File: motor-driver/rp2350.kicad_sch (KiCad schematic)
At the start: 39 parts, among them J2 SM03B-SRSS-TB, U10 W25Q128JVS, U12 NCP1117-3.3_SOT223, U13 RP2350_80QFN, Y1 ABM8-272-T3

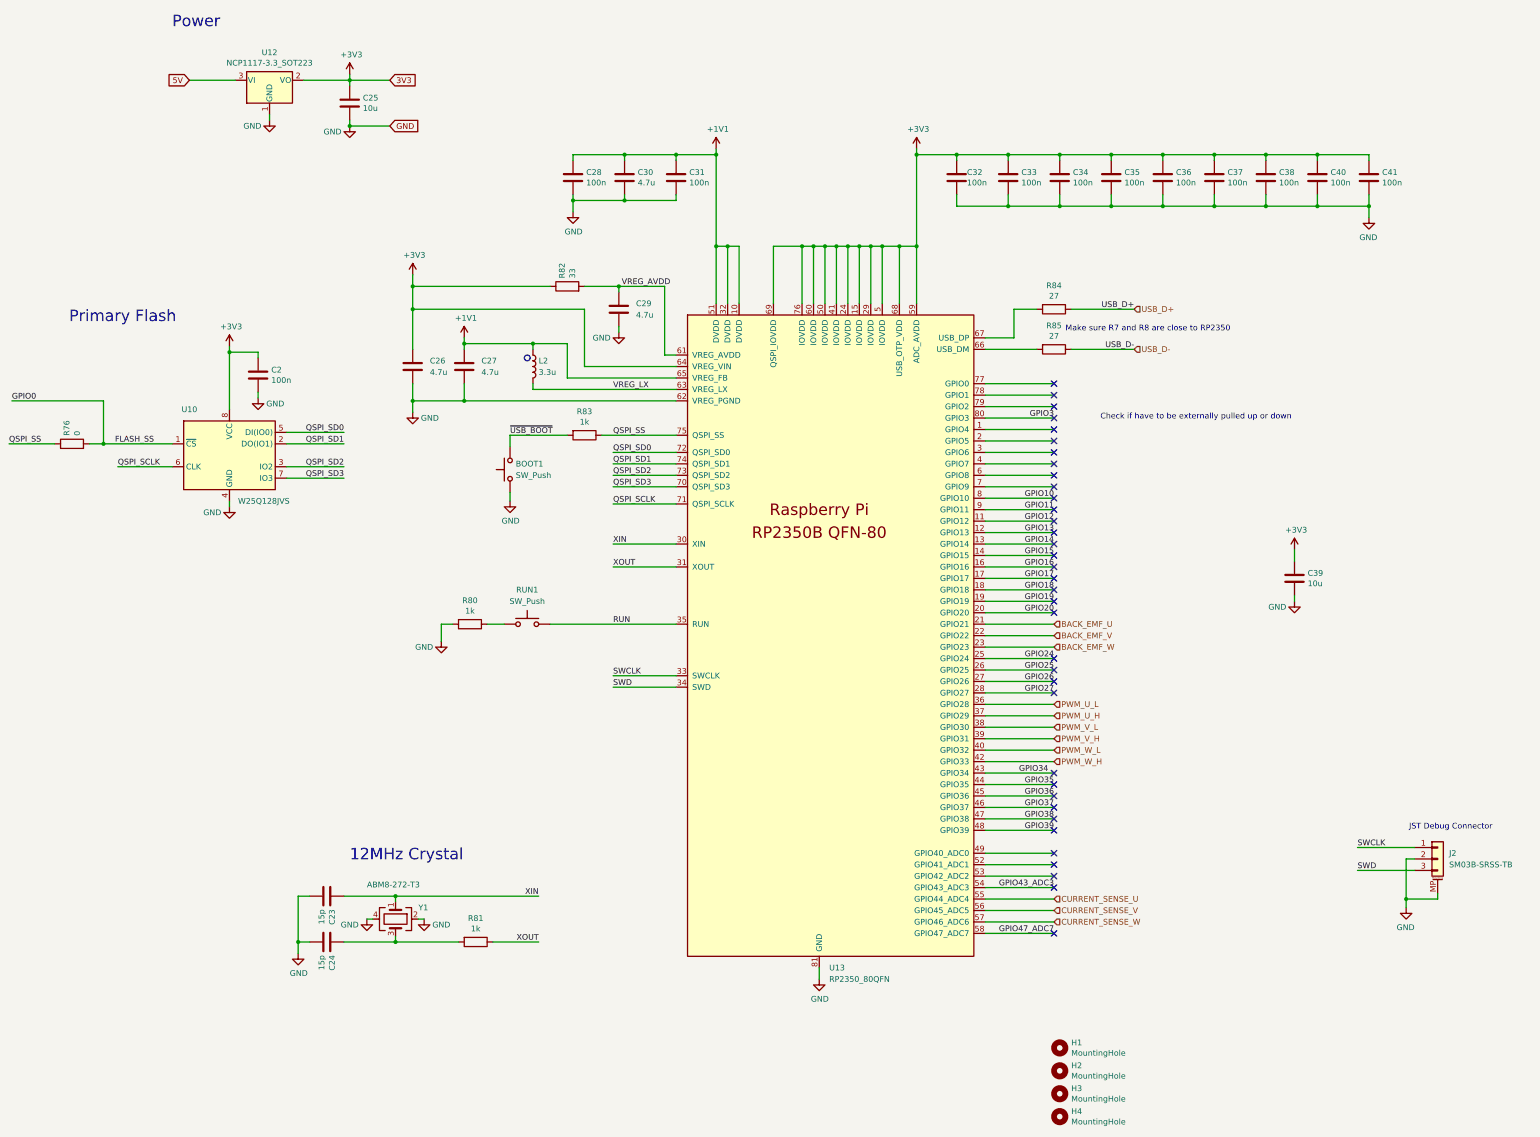
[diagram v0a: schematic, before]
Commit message: added spi connection
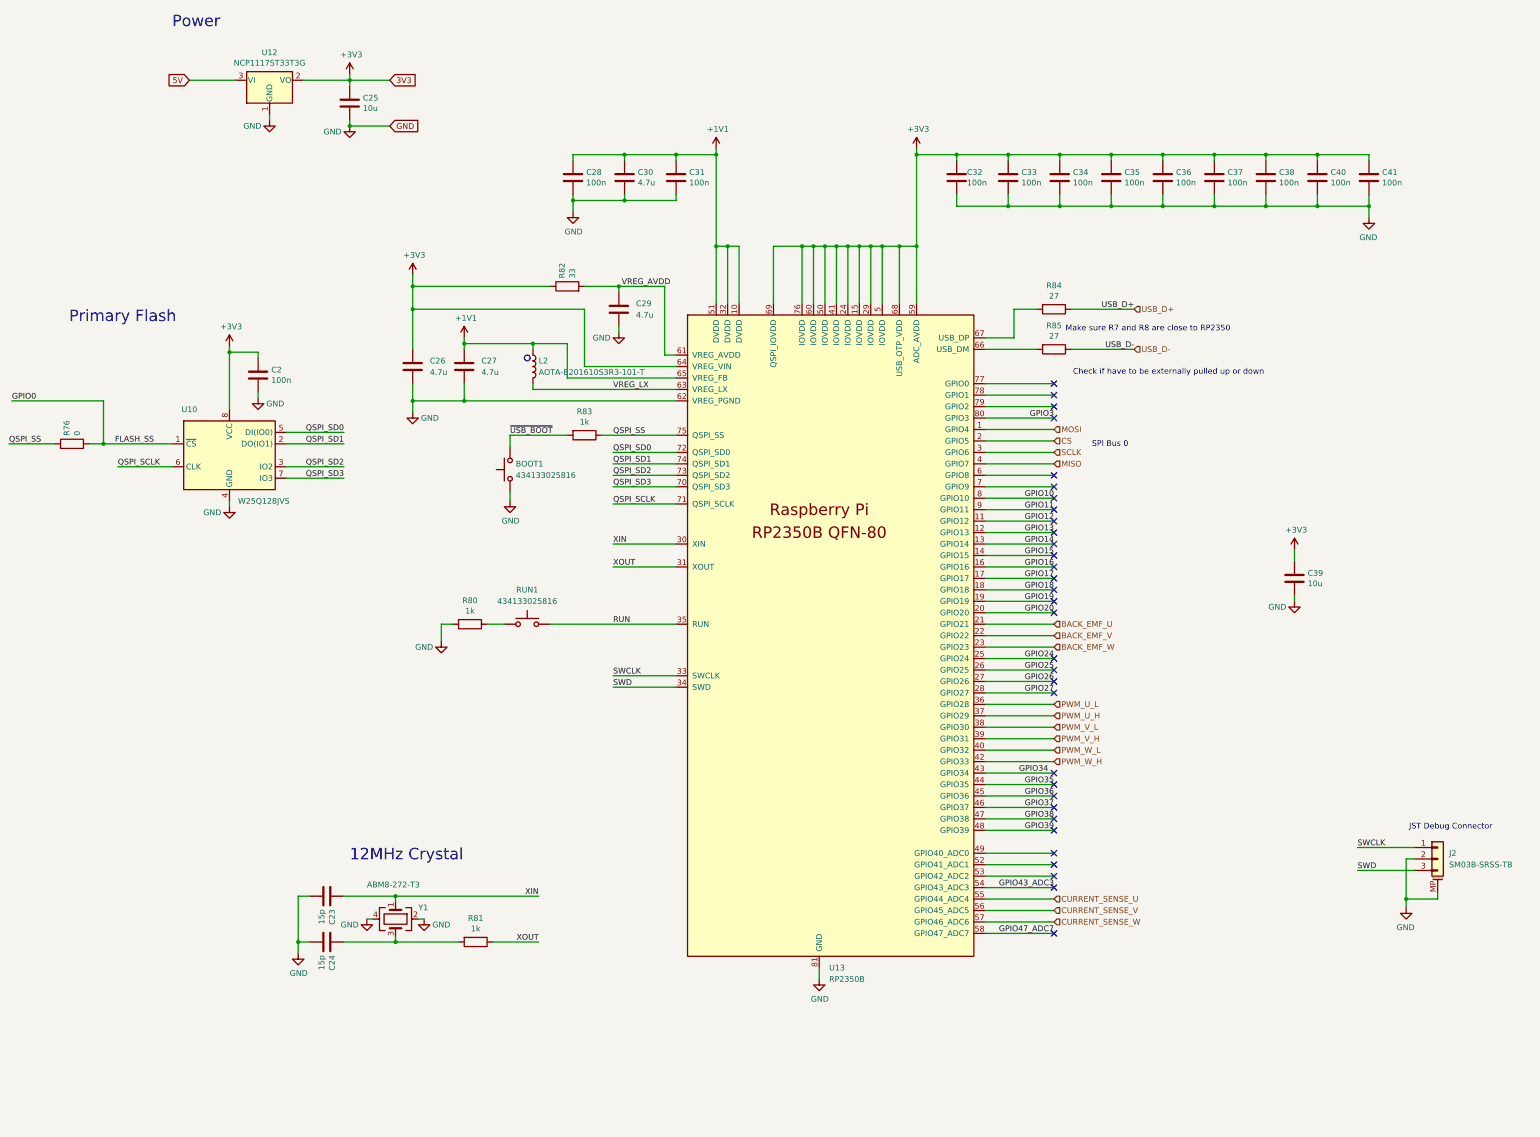
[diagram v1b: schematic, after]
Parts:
- removed H1, H2, H3, H4: MountingHole, MountingHole:MountingHole_2.7mm_M2.5, symbol Mechanical:MountingHole
- BOOT1, RUN1: value SW_Push -> 434133025816
- L2: value 3.3u -> AOTA-B201610S3R3-101-T
- U12: value NCP1117-3.3_SOT223 -> NCP1117ST33T3G
- U13: value RP2350_80QFN -> RP2350B
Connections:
- net MOSI: now reaches U13.1 (GPIO4)
- net CS: now reaches U13.2 (GPIO5)
- net SCLK: now reaches U13.3 (GPIO6)
- net MISO: now reaches U13.4 (GPIO7)
- no-connect marks 36 -> 32
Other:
- note added: "SPI Bus 0"

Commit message: bom finished
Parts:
- BOOT1, RUN1: value 434133025816 -> Button; MANUFACTURER (none) -> Würth Elektronik; MPN (none) -> 434133025816; Supplier (none) -> Digikey
- C2, C28, C31, C32, C33, C34, C35, C36, C37, C38, C40, C41: MANUFACTURER (none) -> KEMET; MPN (none) -> C0402C104K4RACTU; Supplier (none) -> Digikey
- C23, C24: MANUFACTURER (none) -> Murata Electronics; MPN (none) -> GJM1555C1H150GB01D; Supplier (none) -> Digikey
- C25, C39: MANUFACTURER (none) -> Taiyo Yuden; MPN (none) -> LMK107BBJ106MALT; Supplier (none) -> Digikey
- C26, C27, C29, C30: MANUFACTURER (none) -> Samsung Electro-Mechanics; MPN (none) -> CL05A475MP5NRNC; Supplier (none) -> Digikey
- J2: MANUFACTURER (none) -> JST Sales America Inc.; MPN (none) -> SM03B-SRSS-TB
- L2: value AOTA-B201610S3R3-101-T -> 3.3u; MANUFACTURER (none) -> Abracon LLC; MPN (none) -> AOTA-B201610S3R3-101-T; Supplier (none) -> Digikey
- R76: MANUFACTURER (none) -> YAGEO; MPN (none) -> RC0402JR-070RL; Supplier (none) -> Digikey
- R80, R81, R83: MANUFACTURER (none) -> YAGEO; MPN (none) -> RC0402FR-071KL; Supplier (none) -> Digikey
- R82: MANUFACTURER (none) -> YAGEO; MPN (none) -> RC0402JR-0733RL; Supplier (none) -> Digikey
- R84, R85: MANUFACTURER (none) -> YAGEO; MPN (none) -> RC0402JR-0727RL; Supplier (none) -> Digikey
- U12: MANUFACTURER (none) -> onsemi; MPN (none) -> NCP1117ST33T3G; Supplier (none) -> Digikey
- U13: MANUFACTURER (none) -> Raspberry Pi; MPN (none) -> SC1510-A4; Supplier (none) -> Digikey
- Y1: MANUFACTURER (none) -> Abracon LLC; MPN (none) -> ABM8-272-T3; Supplier (none) -> Digikey

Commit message: changed push buttons and zone clearances
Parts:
- removed BOOT1, RUN1: Button, Button_Switch_SMD:SW_Push_1P1T_NO_Vertical_Wuerth_434133025816, symbol Switch:SW_Push
- added BOOT, RUN: KMR221GLFS, KMR221GLFS:SW_KMR221GLFS, symbol KMR221GLFS:KMR221GLFS
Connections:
- net GND: now also BOOT.1, BOOT.4
- net RUN: now also RUN.2, RUN.3
- net ~{USB_BOOT}: now also BOOT.2, BOOT.3
- net at R80.1: now also RUN.1, RUN.4
- no-connect marks 32 -> 34
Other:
- moved on the sheet: R80

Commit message: reoriented parts
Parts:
- C2: footprint Capacitor_SMD:C_0402_1005Metric -> Capacitor_SMD:C_0603_1608Metric
- R76: footprint Resistor_SMD:R_0402_1005Metric -> Resistor_SMD:R_0603_1608Metric
- renumbered BOOT to BOOT1, RUN to RUN1
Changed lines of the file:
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@@
 			)
 		)
-		(property "Footprint" "Capacitor_SMD:C_0402_1005Metric"
+		(property "Footprint" "Capacitor_SMD:C_0603_1608Metric"
 			(at 74.6252 113.665 0)
 			(effects
@@
 		(dnp no)
 		(fields_autoplaced yes)
-		(property "Reference" "RUN"
+		(property "Reference" "RUN1"
 			(at 131.0005 158.75 0)
 			(effects
@@
 			(project ""
 				(path "/2980fc7e-b297-4843-ba9f-cceafa384b2f/fc9ab5c1-5213-4422-8df6-375c5f661fb4"
-					(reference "RUN")
+					(reference "RUN1")
 					(unit 1)
 				)
@@
 		(dnp no)
 		(fields_autoplaced yes)
-		(property "Reference" "BOOT"
+		(property "Reference" "BOOT1"
 			(at 134.62 131.8894 90)
 			(effects
@@
 			(project ""
 				(path "/2980fc7e-b297-4843-ba9f-cceafa384b2f/fc9ab5c1-5213-4422-8df6-375c5f661fb4"
-					(reference "BOOT")
+					(reference "BOOT1")
 					(unit 1)
 				)
@@
 			)
 		)
-		(property "Footprint" "Resistor_SMD:R_0402_1005Metric"
+		(property "Footprint" "Resistor_SMD:R_0603_1608Metric"
 			(at 32.385 126.873 90)
 			(effects
